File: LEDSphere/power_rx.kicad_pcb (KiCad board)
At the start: 2 copper layers, 140 x 140 mm, 46 parts, among them U101 TPS54202DDC, U102 TPS54202DDC, U105 MH253

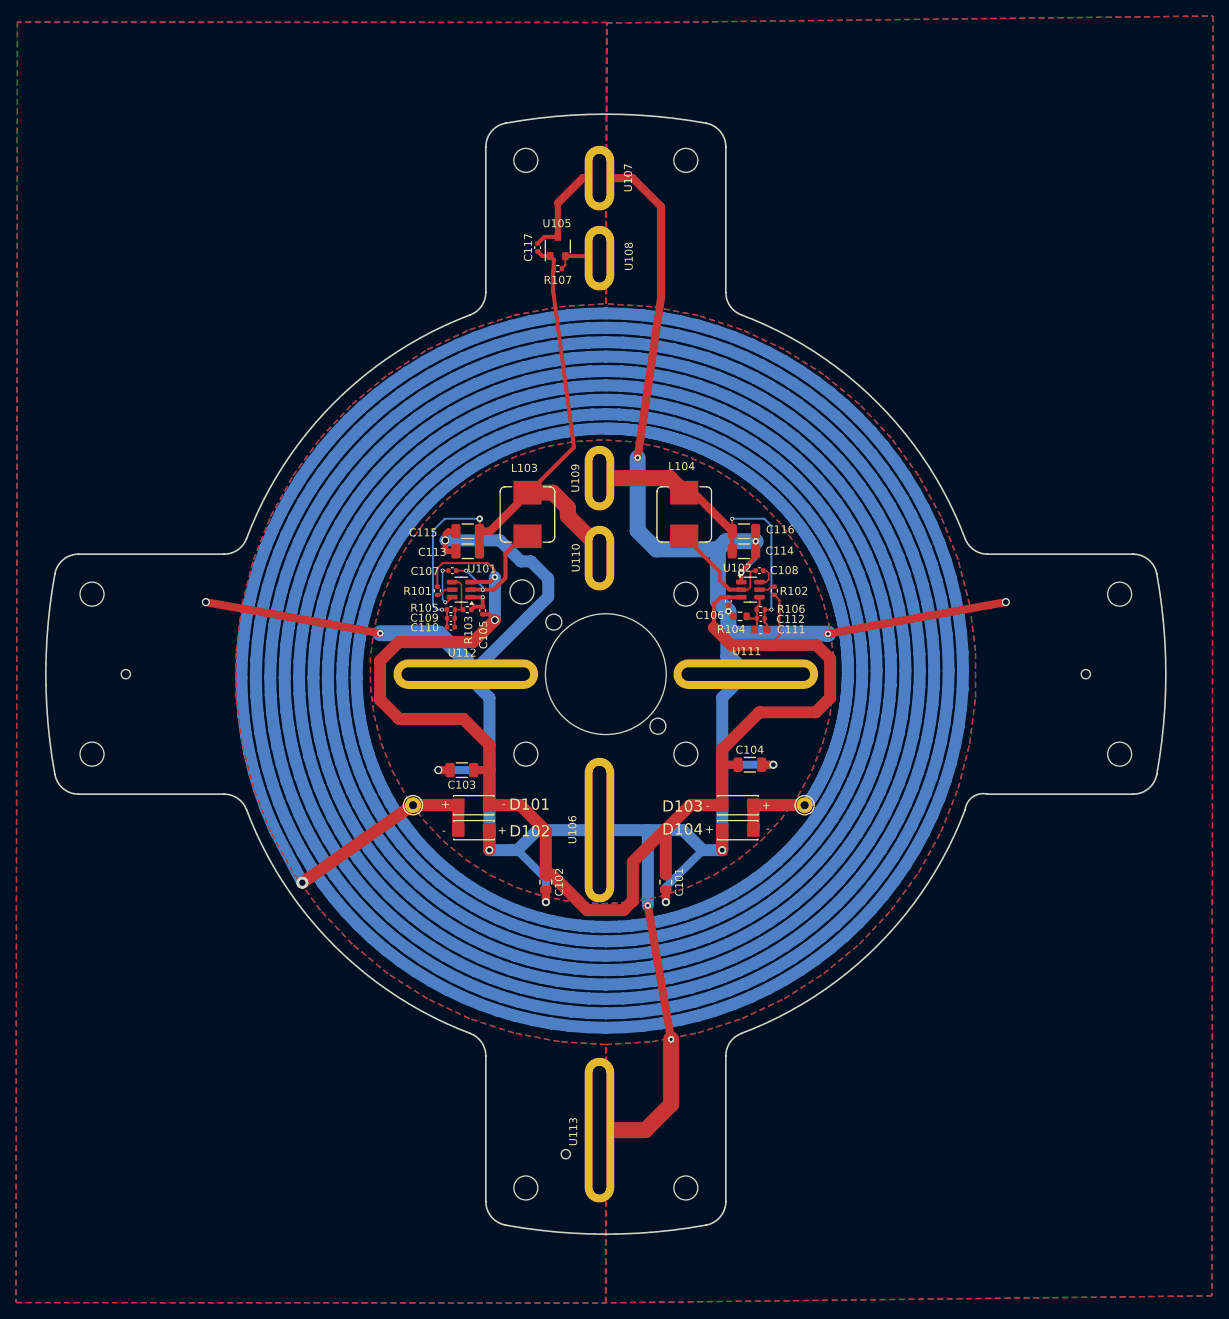
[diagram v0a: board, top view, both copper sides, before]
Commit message: Modify RX Schm. + Adjusted TX Coil
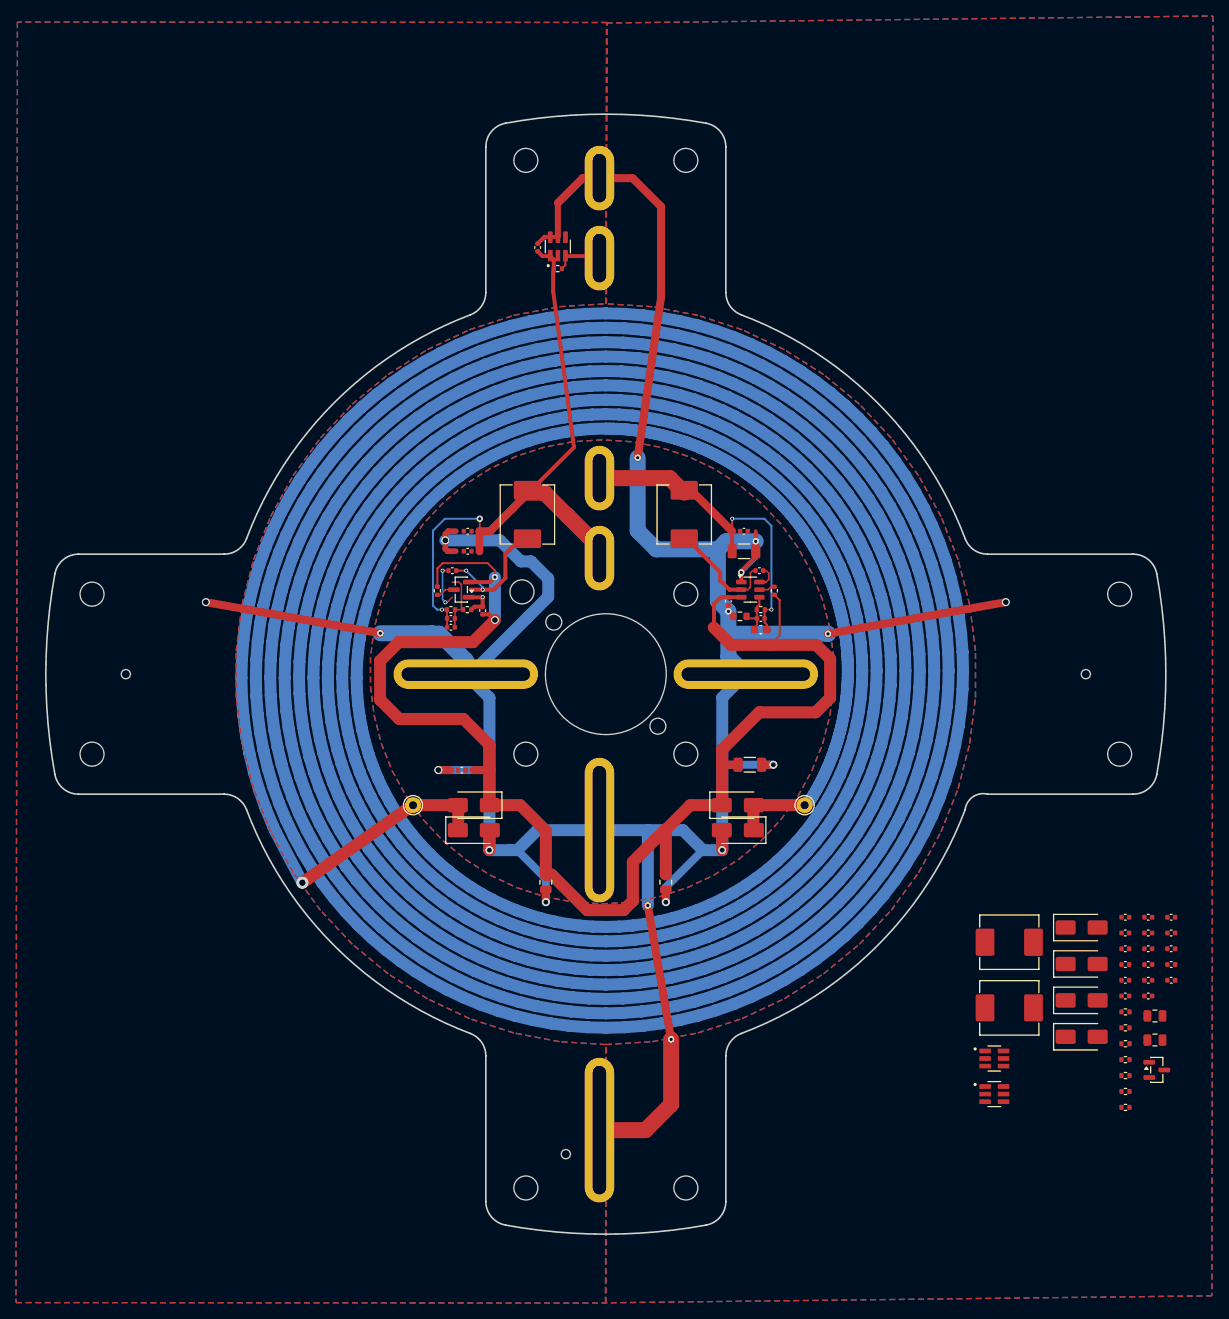
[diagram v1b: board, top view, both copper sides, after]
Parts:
- added C1: 10uF, Capacitor_SMD:C_0402_1005Metric, F.Cu at (159.4, 134.7)
- added C10: 100nF, Capacitor_SMD:C_0402_1005Metric, F.Cu at (162.3, 138.6)
- added C11: 100nF, Capacitor_SMD:C_0402_1005Metric, F.Cu at (162.3, 140.6)
- added C12: 22µF, 25V, Capacitor_SMD:C_0805_2012Metric, F.Cu at (163.1, 150.0)
- added C13: 22uF, Capacitor_SMD:C_0402_1005Metric, F.Cu at (162.3, 142.5)
- added C14: 22uF, Capacitor_SMD:C_0402_1005Metric, F.Cu at (162.3, 144.5)
- added C15: 22uF, Capacitor_SMD:C_0402_1005Metric, F.Cu at (165.2, 134.7)
- added C16: 22uF, Capacitor_SMD:C_0402_1005Metric, F.Cu at (165.2, 136.6)
- added C17: 56pF, Capacitor_SMD:C_0402_1005Metric, F.Cu at (165.2, 138.6)
- added C18: 75pF, Capacitor_SMD:C_0402_1005Metric, F.Cu at (165.2, 140.6)
- added C19: 100nF, Capacitor_SMD:C_0402_1005Metric, F.Cu at (165.2, 142.5)
- added C2: 10uF, Capacitor_SMD:C_0402_1005Metric, F.Cu at (159.4, 136.6)
- added C3: 100nF, Capacitor_SMD:C_0402_1005Metric, F.Cu at (159.4, 138.6)
- added C4: 100nF, Capacitor_SMD:C_0402_1005Metric, F.Cu at (159.4, 140.6)
- added C5: 100nF, Capacitor_SMD:C_0402_1005Metric, F.Cu at (159.4, 142.5)
- added C6: 100nF, Capacitor_SMD:C_0402_1005Metric, F.Cu at (159.4, 144.5)
- added C7: 100nF, Capacitor_SMD:C_0402_1005Metric, F.Cu at (162.3, 134.7)
- added C8: 100nF, Capacitor_SMD:C_0402_1005Metric, F.Cu at (162.3, 136.6)
- added C9: 22µF, 25V, Capacitor_SMD:C_0805_2012Metric, F.Cu at (163.1, 147.0)
- added D1: SS34, Diode_SMD:D_SMA, F.Cu at (154.0, 136.0)
- added D2: SS34, Diode_SMD:D_SMA, F.Cu at (154.0, 140.5)
- added D3: SS34, Diode_SMD:D_SMA, F.Cu at (154.0, 145.1)
- added D4: SS34, Diode_SMD:D_SMA, F.Cu at (154.0, 149.6)
- added L2: 10uH, Inductor_SMD:L_Abracon_ASPI-0630LR, F.Cu at (144.9, 137.8)
- added L3: 15uH, Inductor_SMD:L_Abracon_ASPI-0630LR, F.Cu at (144.9, 146.0)
- added R1: 511k, Resistor_SMD:R_0402_1005Metric, F.Cu at (159.4, 146.5)
- added R2: 511k, Resistor_SMD:R_0402_1005Metric, F.Cu at (159.4, 148.5)
- added R3: 100k, Resistor_SMD:R_0402_1005Metric, F.Cu at (159.4, 150.5)
- added R4: 22.1k, Resistor_SMD:R_0402_1005Metric, F.Cu at (159.4, 152.5)
- added R5: 100k, Resistor_SMD:R_0402_1005Metric, F.Cu at (159.4, 154.5)
- added R6: 13.3k, Resistor_SMD:R_0402_1005Metric, F.Cu at (159.4, 156.4)
- added R7: 20k, Resistor_SMD:R_0402_1005Metric, F.Cu at (159.4, 158.4)
- added U10: DRV5032FCDBZR, Package_TO_SOT_SMD:SOT-23, F.Cu at (163.4, 153.7)
- added U3: TPS54202HDDCR, Footprints:SOT95P280X110-6N, F.Cu at (143.1, 152.3)
- added U4: TPS54202HDDCR, Footprints:SOT95P280X110-6N, F.Cu at (143.1, 156.8)
- C103: value 10µF, 50V -> 100nF; footprint Capacitor_SMD:C_1206_3216Metric -> Capacitor_SMD:C_0402_1005Metric
- C105: value 100nF -> 10uF
- C109: value 47pF -> 100nF
- C113, C115: value 22µF, 25V -> 22uF; footprint Capacitor_SMD:C_1206_3216Metric -> Capacitor_SMD:C_0402_1005Metric
- C116: value 22µF, 25V -> 56pF; footprint Capacitor_SMD:C_1206_3216Metric -> Capacitor_SMD:C_0402_1005Metric
- D101, D102, D103, D104: footprint my_footprints:DIOM7959X265N -> Diode_SMD:D_SMA
- L103: value 33µH -> 10uH; footprint Inductor_SMD:L_Bourns_SRP7028A_7.3x6.6mm -> Inductor_SMD:L_Abracon_ASPI-0630LR
- L104: value 33µH -> 15uH; footprint Inductor_SMD:L_Bourns_SRP7028A_7.3x6.6mm -> Inductor_SMD:L_Abracon_ASPI-0630LR
- R101: value 100k -> 20k
- R103: value 22k -> 511k
- R105: value 100k -> 511k
- U101: value TPS54202DDC -> DRV5032FCDBZR; footprint Package_TO_SOT_SMD:SOT-23-6 -> Package_TO_SOT_SMD:SOT-23
- U105: value MH253 -> TPS54202HDDCR; footprint my_footprints:MH253 -> Footprints:SOT95P280X110-6N
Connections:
- C103 pad 1: /U_unreg -> +3.3V
- C105 pad 1: /U_unreg -> GND
- C105 pad 2: GND -> /U_unreg
- C107 pad 1: /boot_BC1 -> GND
- C107 pad 2: /SW_BC1 -> /U_unreg
- C109 pad 1: +3.3V -> Net-(U105-SW)
- C109 pad 2: /FB_BC1 -> Net-(U105-BOOT)
- C113 pad 1: +3.3V -> GND
- C113 pad 2: GND -> +3.3V
- C115 pad 1: +3.3V -> GND
- C115 pad 2: GND -> +3.3V
- C116 pad 1: +5V -> Net-(U105-FB)
- C116 pad 2: GND -> +3.3V
- D101 pad 2: /coil1 -> /coil2
- D102 pad 1: /coil1 -> /coil2
- L103 pad 1: /SW_BC1 -> Net-(U105-SW)
- L104 pad 1: /SW_BC2 -> Net-(U115-SW)
- R101 pad 1: /U_unreg -> +3.3V
- R101 pad 2: /EN_BC1 -> Hall
- R103 pad 1: GND -> Net-(U115-EN)
- R103 pad 2: /FB_BC1 -> /U_unreg
- R105 pad 1: /FB_BC1 -> Net-(U105-EN)
- R105 pad 2: +3.3V -> /U_unreg
- U101 pad 1: GND -> +3.3V
- U101 pad 2: /SW_BC1 -> Hall
- U101 pad 3: /U_unreg -> GND
- U103 pad 1: /coil1 -> Net-(U103-pin)
- U105 pad 1: +3.3V -> GND
- U105 pad 2: Net-(U105-Output) -> Net-(U105-SW)
- U105 pad 3: GND -> /U_unreg
- U108 pad 1: Net-(U105-Output) -> Hall
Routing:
- net (no net): track 0.00 -> 18.4 mm
- net /SW_BC1: track 16.2 -> 0.00 mm, vias 2 -> 0
- net /boot_BC1: track 5.96 -> 0.00 mm, vias 2 -> 0
- net GND: track 384.3 -> 390.2 mm, vias 18 -> 20
- net /EN_BC1: track 2.13 -> 0.00 mm
- net +3.3V: track 81.1 -> 80.5 mm
- net Hall: vias 0 -> 2

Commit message: first draft rx power layout
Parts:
- removed C101, C102: 22µF, 25V, Capacitor_SMD:C_0805_2012Metric
- removed C103, C106, C107, C108, C109, C117: 100nF, Capacitor_SMD:C_0402_1005Metric
- removed C104: 10µF, 50V, Capacitor_SMD:C_1206_3216Metric
- removed C105: 10uF, Capacitor_SMD:C_0402_1005Metric
- removed C110: 10pF, Capacitor_SMD:C_0402_1005Metric
- removed C111: 30pF, Capacitor_SMD:C_0603_1608Metric
- removed C112: 47pF, Capacitor_SMD:C_0402_1005Metric
- removed C113, C115: 22uF, Capacitor_SMD:C_0402_1005Metric
- removed C114: 22µF, 25V, Capacitor_SMD:C_1206_3216Metric
- removed C116: 56pF, Capacitor_SMD:C_0402_1005Metric
- removed D101, D102, D103, D104: SS34, Diode_SMD:D_SMA
- removed L103: 10uH, Inductor_SMD:L_Abracon_ASPI-0630LR
- removed L104: 15uH, Inductor_SMD:L_Abracon_ASPI-0630LR
- removed R101, R107: 20k, Resistor_SMD:R_0402_1005Metric
- removed R102, R106: 100k, Resistor_SMD:R_0402_1005Metric
- removed R103, R105: 511k, Resistor_SMD:R_0402_1005Metric
- removed R104: 13k, Resistor_SMD:R_0603_1608Metric
- removed U101: DRV5032FCDBZR, Package_TO_SOT_SMD:SOT-23
- removed U102: TPS54202DDC, Package_TO_SOT_SMD:SOT-23-6
- removed U103, U104: ~, my_footprints:Pin_D1.0mm
- removed U105: TPS54202HDDCR, Footprints:SOT95P280X110-6N
- added REF**: COIL_GENERATOR, COIL_GENERATOR, B.Cu at (94.8, 103.1)
- C1, C13, C14, C15, C16, C2: footprint Capacitor_SMD:C_0402_1005Metric -> Capacitor_SMD:C_1206_3216Metric
- C12, C9: footprint Capacitor_SMD:C_0805_2012Metric -> Capacitor_SMD:C_1206_3216Metric
- R3, R4, R5, R6, R7: footprint Resistor_SMD:R_0402_1005Metric -> Resistor_SMD:R_0603_1608Metric
- moved U10 127.2 mm to (86.7, 52.2), turned to 180 degrees
- moved R7 127.1 mm to (89.6, 52.3), turned to 90 degrees
- moved C19 119.4 mm to (85.2, 53.9), turned to 90 degrees
- moved R4 108.6 mm to (74.0, 85.4), turned to -90 degrees
- moved R3 105.1 mm to (75.6, 87.1), turned to -90 degrees
- moved C17 102.4 mm to (77.0, 86.5), turned to -90 degrees
- moved R1 99.6 mm to (81.6, 84.3), turned to -90 degrees
- moved C13 99.3 mm to (77.4, 91.1), turned to 90 degrees
- moved C1 96.3 mm to (77.5, 84.1)
- moved C10 96.1 mm to (79.8, 89.4), turned to 180 degrees
- moved C3 95.8 mm to (80.5, 84.3), turned to -90 degrees
- moved C15 95.1 mm to (80.0, 92.4), turned to 90 degrees
- moved C12 92.9 mm to (77.4, 114.4), turned to -90 degrees
- moved U3 90.8 mm to (79.8, 87.1), turned to 180 degrees
- moved C9 89.3 mm to (80.0, 114.4), turned to -90 degrees
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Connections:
- C5 pad 1: Net-(U1-pin) -> /coil2
- C5 pad 2: /coil2 -> Net-(D1-A)
- C6 pad 1: Net-(U1-pin) -> /coil2
- C6 pad 2: /coil2 -> Net-(D1-A)
- C7 pad 1: Net-(U1-pin) -> /coil2
- C7 pad 2: /coil2 -> Net-(D1-A)
- C8 pad 1: Net-(U1-pin) -> /coil2
- C8 pad 2: /coil2 -> Net-(D1-A)
- D1 pad 2: /coil2 -> Net-(D1-A)
- D2 pad 1: /coil2 -> Net-(D1-A)
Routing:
- net /coil1: track 2103.4 -> 19.3 mm, vias 1 -> 0
- net GND: track 390.2 -> 90.4 mm, vias 20 -> 6
- net /U_unreg: track 179.9 -> 108.2 mm, vias 2 -> 0
- net +5V: track 42.6 -> 20.7 mm, vias 2 -> 0
- net /coil2: track 0.00 -> 21.3 mm
- net (no net): track 18.4 -> 0.00 mm
- net /SW_BC2: track 14.3 -> 0.00 mm
- net +3.3V: track 80.5 -> 66.9 mm, vias 2 -> 0
- net Net-(D1-A): track 0.00 -> 11.4 mm
- net Hall: track 0.00 -> 11.2 mm, vias 2 -> 0
- net Net-(U105-Output): track 10.5 -> 0.00 mm
- net Net-(U4-EN): track 0.00 -> 10.1 mm, vias 0 -> 2
- net Net-(U3-SW): track 0.00 -> 9.59 mm
- net Net-(U4-SW): track 0.00 -> 8.81 mm
- net /FB_BC1: track 7.75 -> 0.00 mm
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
